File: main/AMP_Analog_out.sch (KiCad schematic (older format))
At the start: 11 parts

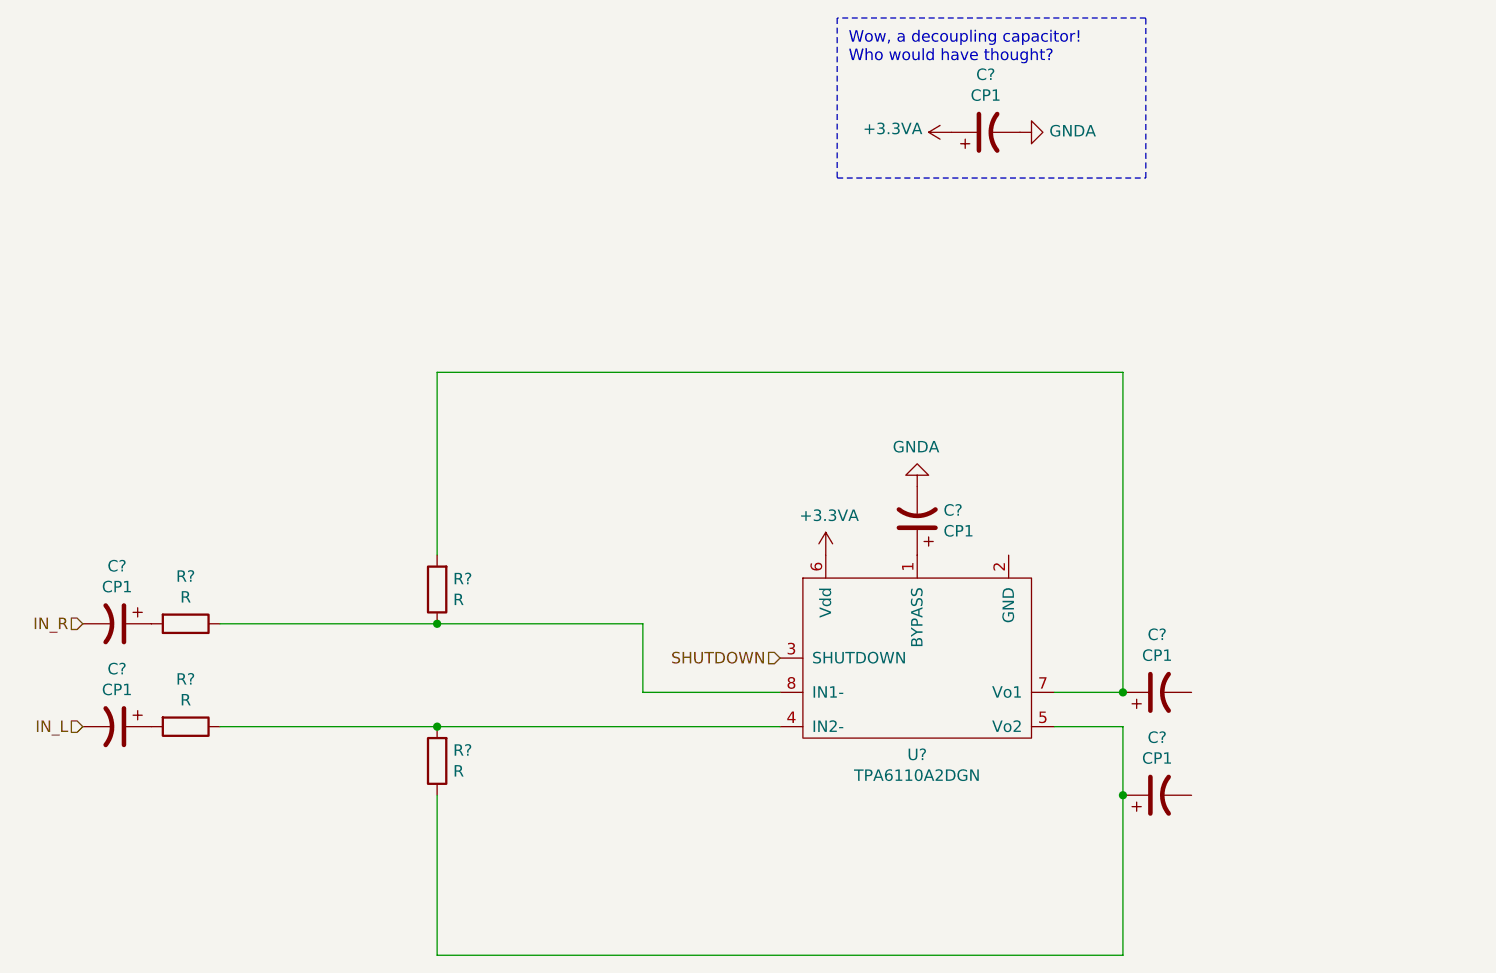
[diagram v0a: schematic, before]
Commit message: Remove old DAC files. Connect amplifier to audio out
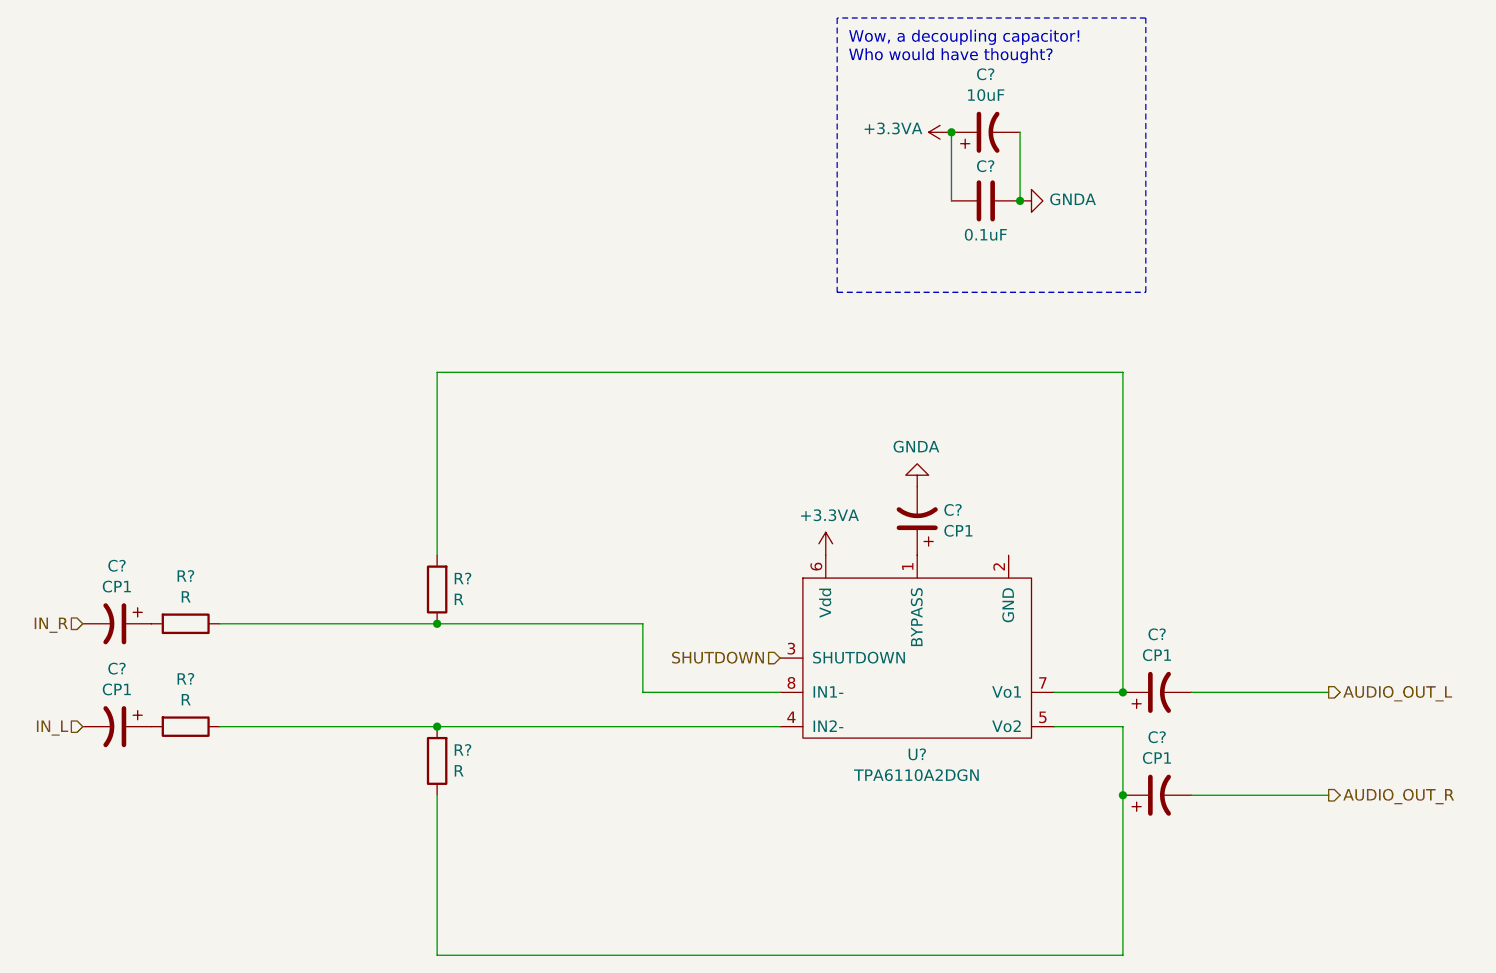
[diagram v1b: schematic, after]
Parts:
- added C?: 0.1uF, symbol Device:C
- C?: value CP1 -> 10uF
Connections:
- net +3.3VA: now also C?.2
- net GNDA: now also C?.1
- net AUDIO_OUT_L: now reaches C?.2
- net AUDIO_OUT_R: now reaches C?.2
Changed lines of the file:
@@
 $Descr A4 11693 8268
 encoding utf-8
-Sheet 7 7
+Sheet 7 6
 Title ""
 Date ""
@@
 L power:GNDA #PWR?
 U 1 1 6144FB76
-P 6450 1550
-F 0 "#PWR?" H 6450 1300 50  0001 C CNN
-F 1 "GNDA" V 6455 1422 50  0000 R CNN
-F 2 "" H 6450 1550 50  0001 C CNN
-F 3 "" H 6450 1550 50  0001 C CNN
-	1    6450 1550
+P 6450 1850
+F 0 "#PWR?" H 6450 1600 50  0001 C CNN
+F 1 "GNDA" V 6455 1722 50  0000 R CNN
+F 2 "" H 6450 1850 50  0001 C CNN
+F 3 "" H 6450 1850 50  0001 C CNN
+	1    6450 1850
 	0    -1   -1   0
 $EndComp
@@
 P 6300 1550
 F 0 "C?" V 6552 1550 50  0000 C CNN
-F 1 "CP1" V 6461 1550 50  0000 C CNN
+F 1 "10uF" V 6461 1550 50  0000 C CNN
 F 2 "" H 6300 1550 50  0001 C CNN
 F 3 "~" H 6300 1550 50  0001 C CNN
@@
 Wow, a decoupling capacitor! \nWho would have thought?\n
 Wire Notes Line
-	5650 1050 5650 1750
-Wire Notes Line
-	5650 1750 7000 1750
-Wire Notes Line
-	7000 1750 7000 1050
+	5650 1050 5650 2250
+Wire Notes Line
+	5650 2250 7000 2250
+Wire Notes Line
+	7000 2250 7000 1050
 Wire Notes Line
 	7000 1050 5650 1050
@@
 Wire Wire Line
 	6900 4450 6900 5150
+$Comp
+L Device:C C?
+U 1 1 6146271B
+P 6300 1850
+F 0 "C?" V 6150 1850 50  0000 C CNN
+F 1 "0.1uF" V 6450 1850 50  0000 C CNN
+F 2 "" H 6338 1700 50  0001 C CNN
+F 3 "~" H 6300 1850 50  0001 C CNN
+	1    6300 1850
+	0    1    1    0
+$EndComp
+Wire Wire Line
+	6150 1850 6150 1550
+Connection ~ 6150 1550
+Wire Wire Line
+	6450 1550 6450 1850
+Connection ~ 6450 1850
+Wire Wire Line
+	7200 4000 7800 4000
+Wire Wire Line
+	7200 4450 7800 4450
+Text HLabel 7800 4000 2    50   Output ~ 0
+AUDIO_OUT_L
+Text HLabel 7800 4450 2    50   Output ~ 0
+AUDIO_OUT_R
 $EndSCHEMATC

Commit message: Add some component values to AMP
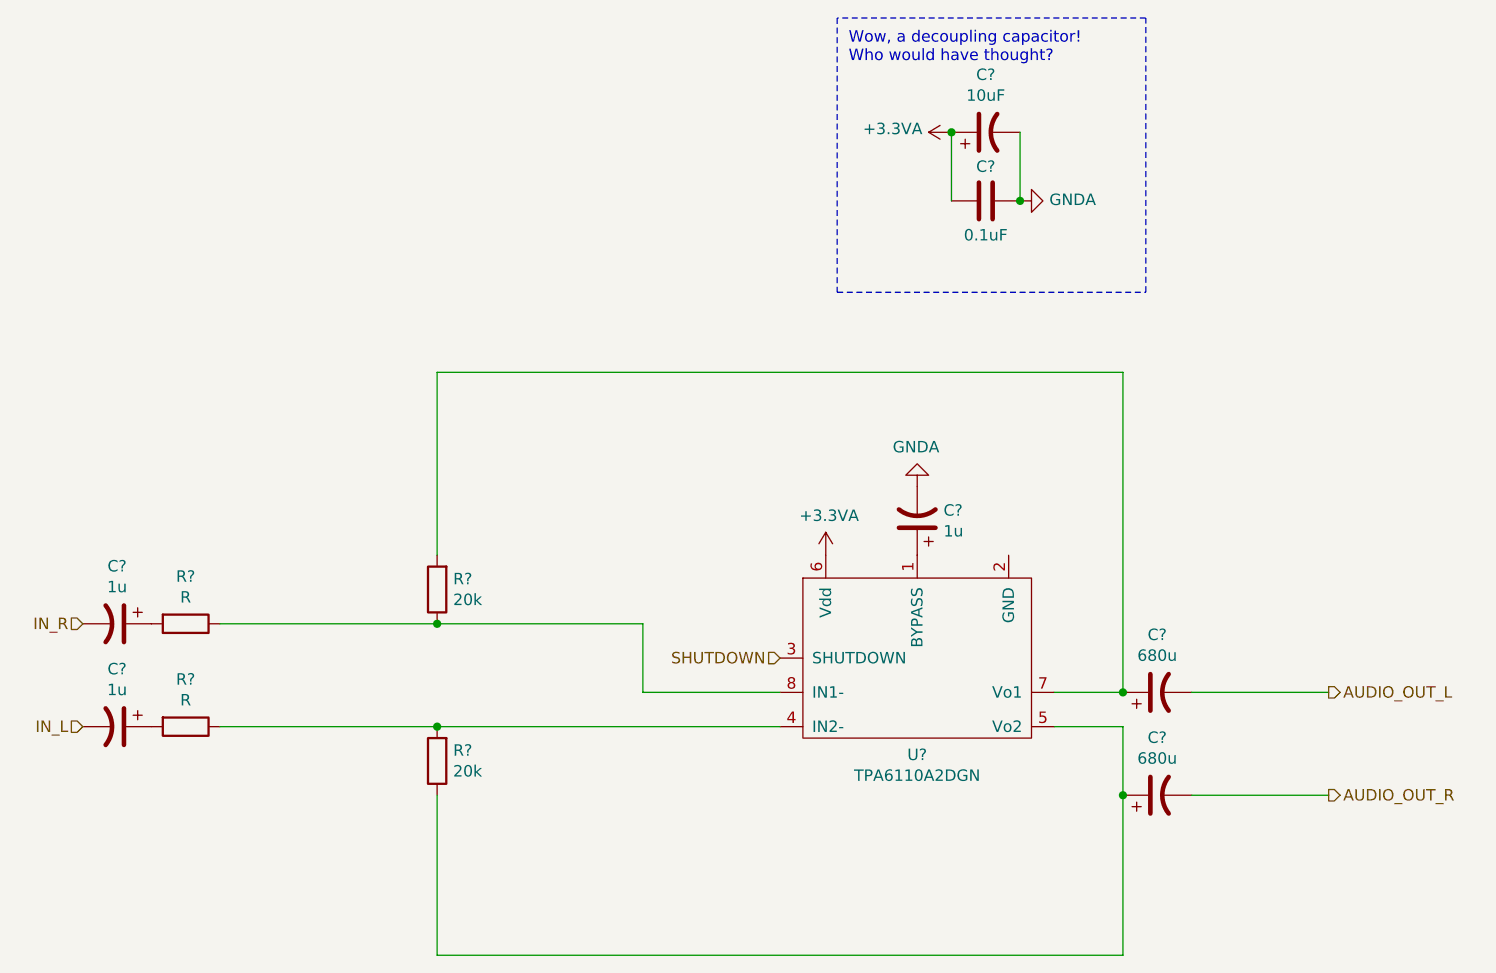
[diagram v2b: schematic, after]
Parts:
- C? (x3): value CP1 -> 1u
- C? (x2): value CP1 -> 680u
- R? (x2): value R -> 20k
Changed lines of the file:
@@
 $Descr A4 11693 8268
 encoding utf-8
-Sheet 7 6
+Sheet 6 6
 Title ""
 Date ""
@@
 P 6000 3250
 F 0 "C?" H 5885 3204 50  0000 R CNN
-F 1 "CP1" H 5885 3295 50  0000 R CNN
+F 1 "1u" H 5885 3295 50  0000 R CNN
 F 2 "" H 6000 3250 50  0001 C CNN
 F 3 "~" H 6000 3250 50  0001 C CNN
@@
 P 2500 3700
 F 0 "C?" V 2248 3700 50  0000 C CNN
-F 1 "CP1" V 2339 3700 50  0000 C CNN
+F 1 "1u" V 2339 3700 50  0000 C CNN
 F 2 "" H 2500 3700 50  0001 C CNN
 F 3 "~" H 2500 3700 50  0001 C CNN
@@
 P 2500 4150
 F 0 "C?" V 2248 4150 50  0000 C CNN
-F 1 "CP1" V 2339 4150 50  0000 C CNN
+F 1 "1u" V 2339 4150 50  0000 C CNN
 F 2 "" H 2500 4150 50  0001 C CNN
 F 3 "~" H 2500 4150 50  0001 C CNN
@@
 P 3900 3550
 F 0 "R?" H 3830 3504 50  0000 R CNN
-F 1 "R" H 3830 3595 50  0000 R CNN
+F 1 "20k" H 3830 3595 50  0000 R CNN
 F 2 "" V 3830 3550 50  0001 C CNN
 F 3 "~" H 3900 3550 50  0001 C CNN
@@
 P 3900 4300
 F 0 "R?" H 3830 4254 50  0000 R CNN
-F 1 "R" H 3830 4345 50  0000 R CNN
+F 1 "20k" H 3830 4345 50  0000 R CNN
 F 2 "" V 3830 4300 50  0001 C CNN
 F 3 "~" H 3900 4300 50  0001 C CNN
@@
 P 7050 4000
 F 0 "C?" V 7302 4000 50  0000 C CNN
-F 1 "CP1" V 7211 4000 50  0000 C CNN
+F 1 "680u" V 7211 4000 50  0000 C CNN
 F 2 "" H 7050 4000 50  0001 C CNN
 F 3 "~" H 7050 4000 50  0001 C CNN
@@
 P 7050 4450
 F 0 "C?" V 7302 4450 50  0000 C CNN
-F 1 "CP1" V 7211 4450 50  0000 C CNN
+F 1 "680u" V 7211 4450 50  0000 C CNN
 F 2 "" H 7050 4450 50  0001 C CNN
 F 3 "~" H 7050 4450 50  0001 C CNN

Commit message: Set up switching regulator circuits.
We only use half of the switching regulator that generates the 1V0
voltage. I'm not sure if the half not being used is connected correctly.
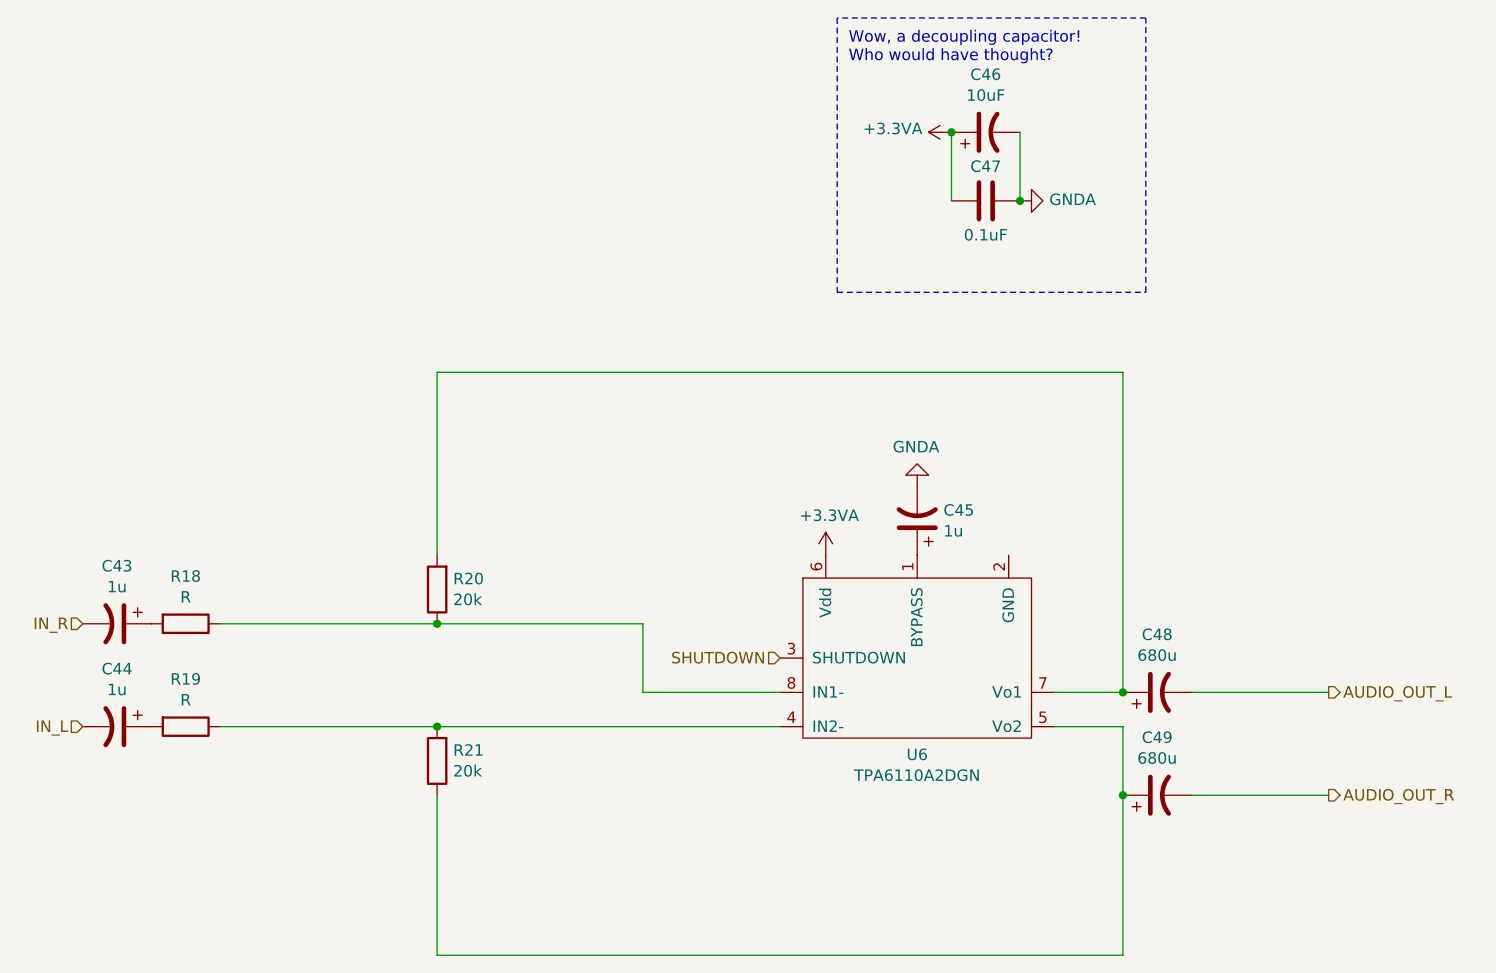
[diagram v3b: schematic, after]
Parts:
- gave numbers to parts that had none: 12
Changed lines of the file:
@@
 $Descr A4 11693 8268
 encoding utf-8
-Sheet 6 6
+Sheet 6 7
 Title ""
 Date ""
@@
 $EndDescr
 $Comp
-L TPA6110A2DGN:TPA6110A2DGN U?
+L TPA6110A2DGN:TPA6110A2DGN U6
 U 1 1 614497DA
 P 6000 3850
-F 0 "U?" H 6000 3427 50  0000 C CNN
+F 0 "U6" H 6000 3427 50  0000 C CNN
 F 1 "TPA6110A2DGN" H 6000 3336 50  0000 C CNN
 F 2 "" H 5650 3750 50  0001 C CNN
@@
 SHUTDOWN
 $Comp
-L power:+3.3VA #PWR?
+L power:+3.3VA #PWR0154
 U 1 1 6144EAAF
 P 5600 3400
-F 0 "#PWR?" H 5600 3250 50  0001 C CNN
+F 0 "#PWR0154" H 5600 3250 50  0001 C CNN
 F 1 "+3.3VA" H 5615 3573 50  0000 C CNN
 F 2 "" H 5600 3400 50  0001 C CNN
@@
 $EndComp
 $Comp
-L power:GNDA #PWR?
+L power:GNDA #PWR0155
 U 1 1 6144FB76
 P 6450 1850
-F 0 "#PWR?" H 6450 1600 50  0001 C CNN
+F 0 "#PWR0155" H 6450 1600 50  0001 C CNN
 F 1 "GNDA" V 6455 1722 50  0000 R CNN
 F 2 "" H 6450 1850 50  0001 C CNN
@@
 $EndComp
 $Comp
-L power:GNDA #PWR?
+L power:GNDA #PWR0156
 U 1 1 61450313
 P 6000 3100
-F 0 "#PWR?" H 6000 2850 50  0001 C CNN
+F 0 "#PWR0156" H 6000 2850 50  0001 C CNN
 F 1 "GNDA" H 6005 2927 50  0000 C CNN
 F 2 "" H 6000 3100 50  0001 C CNN
@@
 $EndComp
 $Comp
-L Device:CP1 C?
+L Device:CP1 C45
 U 1 1 61450A21
 P 6000 3250
-F 0 "C?" H 5885 3204 50  0000 R CNN
+F 0 "C45" H 5885 3204 50  0000 R CNN
 F 1 "1u" H 5885 3295 50  0000 R CNN
 F 2 "" H 6000 3250 50  0001 C CNN
@@
 $EndComp
 $Comp
-L power:+3.3VA #PWR?
+L power:+3.3VA #PWR0157
 U 1 1 614535B7
 P 6150 1550
-F 0 "#PWR?" H 6150 1400 50  0001 C CNN
+F 0 "#PWR0157" H 6150 1400 50  0001 C CNN
 F 1 "+3.3VA" V 6165 1677 50  0000 L CNN
 F 2 "" H 6150 1550 50  0001 C CNN
@@
 $EndComp
 $Comp
-L Device:CP1 C?
+L Device:CP1 C46
 U 1 1 61453C17
 P 6300 1550
-F 0 "C?" V 6552 1550 50  0000 C CNN
+F 0 "C46" V 6552 1550 50  0000 C CNN
 F 1 "10uF" V 6461 1550 50  0000 C CNN
 F 2 "" H 6300 1550 50  0001 C CNN
@@
 	7000 1050 5650 1050
 $Comp
-L Device:CP1 C?
+L Device:CP1 C43
 U 1 1 61459645
 P 2500 3700
-F 0 "C?" V 2248 3700 50  0000 C CNN
+F 0 "C43" V 2248 3700 50  0000 C CNN
 F 1 "1u" V 2339 3700 50  0000 C CNN
 F 2 "" H 2500 3700 50  0001 C CNN
@@
 $EndComp
 $Comp
-L Device:CP1 C?
+L Device:CP1 C44
 U 1 1 6145AB50
 P 2500 4150
-F 0 "C?" V 2248 4150 50  0000 C CNN
+F 0 "C44" V 2248 4150 50  0000 C CNN
 F 1 "1u" V 2339 4150 50  0000 C CNN
 F 2 "" H 2500 4150 50  0001 C CNN
@@
 $EndComp
 $Comp
-L Device:R R?
+L Device:R R18
 U 1 1 6145F753
 P 2800 3700
-F 0 "R?" V 2593 3700 50  0000 C CNN
+F 0 "R18" V 2593 3700 50  0000 C CNN
 F 1 "R" V 2684 3700 50  0000 C CNN
 F 2 "" V 2730 3700 50  0001 C CNN
@@
 $EndComp
 $Comp
-L Device:R R?
+L Device:R R19
 U 1 1 614603F8
 P 2800 4150
-F 0 "R?" V 2593 4150 50  0000 C CNN
+F 0 "R19" V 2593 4150 50  0000 C CNN
 F 1 "R" V 2684 4150 50  0000 C CNN
 F 2 "" V 2730 4150 50  0001 C CNN
@@
 	2950 4150 3900 4150
 $Comp
-L Device:R R?
+L Device:R R20
 U 1 1 6146A9F3
 P 3900 3550
-F 0 "R?" H 3830 3504 50  0000 R CNN
+F 0 "R20" H 3830 3504 50  0000 R CNN
 F 1 "20k" H 3830 3595 50  0000 R CNN
 F 2 "" V 3830 3550 50  0001 C CNN
@@
 	3900 3700 4800 3700
 $Comp
-L Device:R R?
+L Device:R R21
 U 1 1 6146B124
 P 3900 4300
-F 0 "R?" H 3830 4254 50  0000 R CNN
+F 0 "R21" H 3830 4254 50  0000 R CNN
 F 1 "20k" H 3830 4345 50  0000 R CNN
 F 2 "" V 3830 4300 50  0001 C CNN
@@
 	3900 5150 3900 4450
 $Comp
-L Device:CP1 C?
+L Device:CP1 C48
 U 1 1 6146CB5D
 P 7050 4000
-F 0 "C?" V 7302 4000 50  0000 C CNN
+F 0 "C48" V 7302 4000 50  0000 C CNN
 F 1 "680u" V 7211 4000 50  0000 C CNN
 F 2 "" H 7050 4000 50  0001 C CNN
@@
 Connection ~ 6900 4000
 $Comp
-L Device:CP1 C?
+L Device:CP1 C49
 U 1 1 6146D43E
 P 7050 4450
-F 0 "C?" V 7302 4450 50  0000 C CNN
+F 0 "C49" V 7302 4450 50  0000 C CNN
 F 1 "680u" V 7211 4450 50  0000 C CNN
 F 2 "" H 7050 4450 50  0001 C CNN
@@
 	6900 4450 6900 5150
 $Comp
-L Device:C C?
+L Device:C C47
 U 1 1 6146271B
 P 6300 1850
-F 0 "C?" V 6150 1850 50  0000 C CNN
+F 0 "C47" V 6150 1850 50  0000 C CNN
 F 1 "0.1uF" V 6450 1850 50  0000 C CNN
 F 2 "" H 6338 1700 50  0001 C CNN

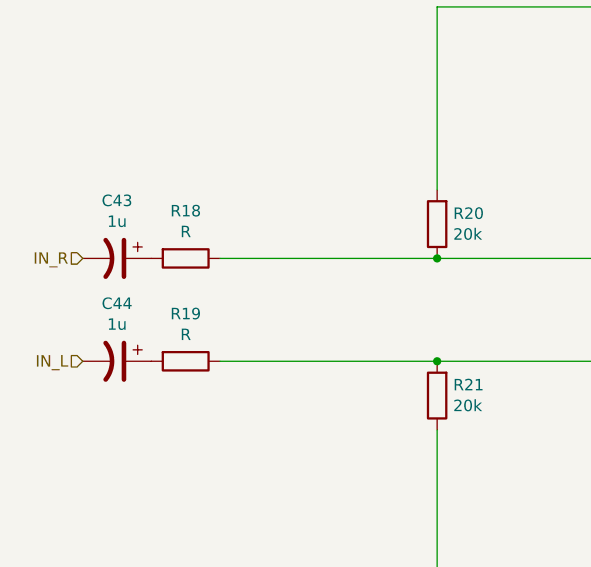
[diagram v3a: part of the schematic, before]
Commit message: Continue wiring of the MCU
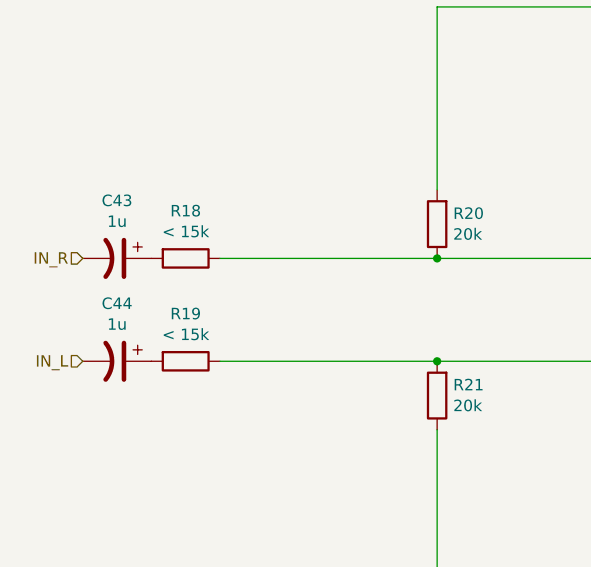
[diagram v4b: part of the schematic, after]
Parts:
- R18, R19: value R -> < 15k
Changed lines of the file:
@@
 P 2800 3700
 F 0 "R18" V 2593 3700 50  0000 C CNN
-F 1 "R" V 2684 3700 50  0000 C CNN
+F 1 "< 15k" V 2684 3700 50  0000 C CNN
 F 2 "" V 2730 3700 50  0001 C CNN
 F 3 "~" H 2800 3700 50  0001 C CNN
@@
 P 2800 4150
 F 0 "R19" V 2593 4150 50  0000 C CNN
-F 1 "R" V 2684 4150 50  0000 C CNN
+F 1 "< 15k" V 2684 4150 50  0000 C CNN
 F 2 "" V 2730 4150 50  0001 C CNN
 F 3 "~" H 2800 4150 50  0001 C CNN
